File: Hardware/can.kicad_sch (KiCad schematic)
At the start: 9 parts, among them U2 SN65HVD230

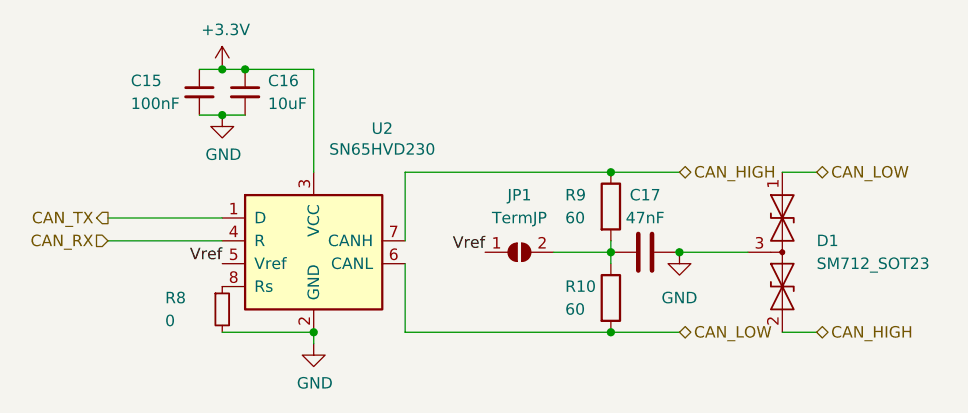
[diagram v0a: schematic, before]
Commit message: added high side switch
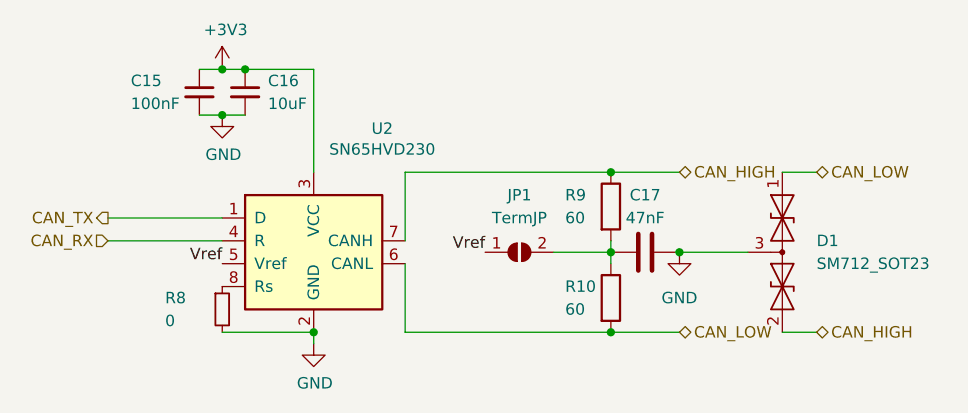
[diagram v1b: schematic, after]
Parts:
- R8: footprint Resistor_SMD:R_0603_1608Metric -> Resistor_SMD:R_0402_1005Metric

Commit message: files
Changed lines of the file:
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@@
 (kicad_sch
-	(version 20231120)
+	(version 20250114)
 	(generator "eeschema")
-	(generator_version "8.0")
+	(generator_version "9.0")
 	(paper "A4")
 	(junction
@@
 	(label "Vref"
 		(at 124.46 90.17 180)
-		(fields_autoplaced yes)
 		(effects
 			(font
@@
 	(label "Vref"
 		(at 153.67 88.9 180)
-		(fields_autoplaced yes)
 		(effects
 			(font
@@
 		(shape input)
 		(at 111.76 87.63 180)
-		(fields_autoplaced yes)
 		(effects
 			(font
@@
 		(shape bidirectional)
 		(at 175.26 80.01 0)
-		(fields_autoplaced yes)
 		(effects
 			(font
@@
 		(shape output)
 		(at 111.76 85.09 180)
-		(fields_autoplaced yes)
 		(effects
 			(font
@@
 		(shape bidirectional)
 		(at 190.5 97.79 0)
-		(fields_autoplaced yes)
 		(effects
 			(font
@@
 		(shape bidirectional)
 		(at 190.5 80.01 0)
-		(fields_autoplaced yes)
 		(effects
 			(font
@@
 		(shape bidirectional)
 		(at 175.26 97.79 0)
-		(fields_autoplaced yes)
-		(effects
-			(font
+		(effects
+			(font

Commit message: tidied up schematic and bom
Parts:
- JP601: renamed from JP1; now left out of the parts list
- R601: renamed from R8; value 0 -> 0Ω
- R602: renamed from R9; value 60 -> 60Ω
- R603: renamed from R10; value 60 -> 60Ω
- renumbered C15 to C601, C16 to C602, C17 to C603, D1 to D601, U2 to U601
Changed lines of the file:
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@@
 		(dnp no)
 		(fields_autoplaced yes)
-		(property "Reference" "#PWR026"
+		(property "Reference" "#PWR0603"
 			(at 134.62 105.41 0)
 			(effects
@@
 			(project "flintandsteel"
 				(path "/7db990e4-92e1-4f99-b4d2-435bbec1ba83/00000000-0000-0000-0000-000061942b9a"
-					(reference "#PWR026")
+					(reference "#PWR0603")
 					(unit 1)
 				)
@@
 		(dnp no)
 		(fields_autoplaced yes)
-		(property "Reference" "#PWR024"
+		(property "Reference" "#PWR0601"
 			(at 124.46 72.39 0)
 			(effects
@@
 			(project "flintandsteel"
 				(path "/7db990e4-92e1-4f99-b4d2-435bbec1ba83/00000000-0000-0000-0000-000061942b9a"
-					(reference "#PWR024")
+					(reference "#PWR0601")
 					(unit 1)
 				)
@@
 		(dnp no)
 		(fields_autoplaced yes)
-		(property "Reference" "U2"
+		(property "Reference" "U601"
 			(at 142.24 75.1586 0)
 			(effects
@@
 			(project "flintandsteel"
 				(path "/7db990e4-92e1-4f99-b4d2-435bbec1ba83/00000000-0000-0000-0000-000061942b9a"
-					(reference "U2")
+					(reference "U601")
 					(unit 1)
 				)
@@
 		(dnp no)
 		(fields_autoplaced yes)
-		(property "Reference" "C16"
+		(property "Reference" "C602"
 			(at 129.54 69.8562 0)
 			(effects
@@
 			(project "flintandsteel"
 				(path "/7db990e4-92e1-4f99-b4d2-435bbec1ba83/00000000-0000-0000-0000-000061942b9a"
-					(reference "C16")
+					(reference "C602")
 					(unit 1)
 				)
@@
 		(dnp no)
 		(fields_autoplaced yes)
-		(property "Reference" "D1"
+		(property "Reference" "D601"
 			(at 190.5 87.63 90)
 			(effects
@@
 			(project "flintandsteel"
 				(path "/7db990e4-92e1-4f99-b4d2-435bbec1ba83/00000000-0000-0000-0000-000061942b9a"
-					(reference "D1")
+					(reference "D601")
 					(unit 1)
 				)
@@
 		(dnp no)
 		(fields_autoplaced yes)
-		(property "Reference" "#PWR027"
+		(property "Reference" "#PWR0604"
 			(at 175.26 95.25 0)
 			(effects
@@
 			(project "flintandsteel"
 				(path "/7db990e4-92e1-4f99-b4d2-435bbec1ba83/00000000-0000-0000-0000-000061942b9a"
-					(reference "#PWR027")
+					(reference "#PWR0604")
 					(unit 1)
 				)
@@
 		(dnp no)
 		(fields_autoplaced yes)
-		(property "Reference" "C15"
+		(property "Reference" "C601"
 			(at 114.3 69.85 0)
 			(effects
@@
 			(project "flintandsteel"
 				(path "/7db990e4-92e1-4f99-b4d2-435bbec1ba83/00000000-0000-0000-0000-000061942b9a"
-					(reference "C15")
+					(reference "C601")
 					(unit 1)
 				)
@@
 		(on_board yes)
 		(dnp no)
-		(property "Reference" "R8"
+		(property "Reference" "R601"
 			(at 118.11 93.98 0)
 			(effects
@@
 			)
 		)
-		(property "Value" "0"
+		(property "Value" "0Ω"
 			(at 118.11 96.52 0)
 			(effects
@@
 			(project "flintandsteel"
 				(path "/7db990e4-92e1-4f99-b4d2-435bbec1ba83/00000000-0000-0000-0000-000061942b9a"
-					(reference "R8")
+					(reference "R601")
 					(unit 1)
 				)
@@
 		(dnp no)
 		(fields_autoplaced yes)
-		(property "Reference" "R10"
+		(property "Reference" "R603"
 			(at 162.56 92.71 0)
 			(effects
@@
 			)
 		)
-		(property "Value" "60"
+		(property "Value" "60Ω"
 			(at 162.56 95.25 0)
 			(effects
@@
 			(project "flintandsteel"
 				(path "/7db990e4-92e1-4f99-b4d2-435bbec1ba83/00000000-0000-0000-0000-000061942b9a"
-					(reference "R10")
+					(reference "R603")
 					(unit 1)
 				)
@@
 		(dnp no)
 		(fields_autoplaced yes)
-		(property "Reference" "R9"
+		(property "Reference" "R602"
 			(at 162.56 82.55 0)
 			(effects
@@
 			)
 		)
-		(property "Value" "60"
+		(property "Value" "60Ω"
 			(at 162.56 85.09 0)
 			(effects
@@
 			(project "flintandsteel"
 				(path "/7db990e4-92e1-4f99-b4d2-435bbec1ba83/00000000-0000-0000-0000-000061942b9a"
-					(reference "R9")
+					(reference "R602")
 					(unit 1)
 				)
@@
 		(dnp no)
 		(fields_autoplaced yes)
-		(property "Reference" "C17"
+		(property "Reference" "C603"
 			(at 171.45 82.55 90)
 			(effects
@@
 			(project "flintandsteel"
 				(path "/7db990e4-92e1-4f99-b4d2-435bbec1ba83/00000000-0000-0000-0000-000061942b9a"
-					(reference "C17")
+					(reference "C603")
 					(unit 1)
 				)
@@
 		(dnp no)
 		(fields_autoplaced yes)
-		(property "Reference" "#PWR025"
+		(property "Reference" "#PWR0602"
 			(at 124.46 80.01 0)
 			(effects
@@
 			(project "flintandsteel"
 				(path "/7db990e4-92e1-4f99-b4d2-435bbec1ba83/00000000-0000-0000-0000-000061942b9a"
-					(reference "#PWR025")
+					(reference "#PWR0602")
 					(unit 1)
 				)
@@
 		(unit 1)
 		(exclude_from_sim no)
-		(in_bom yes)
-		(on_board yes)
-		(dnp no)
-		(fields_autoplaced yes)
-		(property "Reference" "JP1"
+		(in_bom no)
+		(on_board yes)
+		(dnp no)
+		(fields_autoplaced yes)
+		(property "Reference" "JP601"
 			(at 157.48 82.55 0)
 			(effects
@@
 			(project "flintandsteel"
 				(path "/7db990e4-92e1-4f99-b4d2-435bbec1ba83/00000000-0000-0000-0000-000061942b9a"
-					(reference "JP1")
-					(unit 1)
-				)
+					(reference "JP601")
+					(unit 1)
+				)
